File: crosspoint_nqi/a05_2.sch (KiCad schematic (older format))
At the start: 48 parts, among them U5022 74HC04, U5034 74HC27, U5035 74LVC07, U5036 74HC02, U5037 74HC4002, U5038 74HC02, U5039 74HC27, U5040 74HC27, U5041 74LVC07, U5042 74HC02, U5043 74HC27, U5044 74HC02, U5045 74HC27, U5046 74LVC07, U5047 74HC02, U5048 74HC27, U5049 74HC02, U5050 74HC02, U5051 74LVC07, U5052 74HC02, U5053 74HC02, U5054 74HC02, U5055 74HC4002, U5056 74HC27, U5057 74HC02, U5058 74LVC07, U5059 74HC04, U5060 74HC02, U5061 74LVC07, U5062 74HC02, U5063 74HC27, U5064 74HC27, U5065 74HC27, U5066 74HC02, U5067 74LVC07, U5068 74HC02, U5069 74HC27, U5070 74HC02

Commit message: Tied in module 6 and corrected a handful of naming/routing errors... most notably some missing gates from A06-1
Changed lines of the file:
@@
 	1    0    0    -1
 $EndComp
-Text Label 5650 10100 0    60   ~ 0
-5XP15
 Text Notes 5650 10200 0    60   ~ 0
 RG,WQ
@@
 	1    0    0    -1
 $EndComp
-Text Label 15800 4400 0    60   ~ 0
-6XP8
 Text Notes 15600 4550 0    60   ~ 0
 RU,WG,WSC,TOV
@@
 	16350 1350 17100 1350
 Connection ~ 16350 9300
+Wire Wire Line
+	5700 10100 5700 10000
+Wire Wire Line
+	5700 10000 5750 10000
+Connection ~ 5700 10100
+Text HLabel 5750 10000 2    60   Output ~ 0
+5XP15
+Wire Wire Line
+	15850 4400 15850 4300
+Wire Wire Line
+	15850 4300 15950 4300
+Connection ~ 15850 4400
+Text HLabel 15950 4300 2    60   Output ~ 0
+6XP8
 $EndSCHEMATC

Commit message: Tied in module 7, and corrected lots of errors.
Off the top of my head:
* T12DC/ not actually connected to restart logic in A02-2
* IC12/ and IC13 schematic errors
* Lots of gates moved from later modules up to modules 2-7
* YT0..7 logic dropped from 7, it belongs in 14
* Lots of missing signal breakouts
* ...probably some other things, I should keep a list as I go

All control pulses associated with GOJ1 now behave correctly during
GOJ1.
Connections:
- net CHINC/: now also U5049.8
- net T05/: now also U5044.12, U5044.9, U5047.12, U5047.3, U5047.9, U5049.12, U5049.3, U5049.6, U5049.9, U5050.3, U5050.6
- net RL10BB: now reaches U5034.9, U5036.10
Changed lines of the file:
@@
 Text HLabel 14300 7050 0    60   Input ~ 0
 MONWBK
-Text Label 16150 7050 2    60   ~ 0
-U2BBK
 $Comp
 L 74HC02 U5062
@@
 	4050 900  4450 900
 Wire Wire Line
-	6500 1000 5650 1000
+	5650 1000 6500 1000
 Wire Wire Line
 	8600 1150 8750 1150
@@
 	5650 6050 5650 6050
 Wire Wire Line
-	4400 7000 4400 11700
+	4400 5950 4400 11700
 Wire Wire Line
 	4400 6650 4450 6650
@@
 Connection ~ 4400 10200
 Wire Wire Line
-	4100 3150 4100 11500
+	4100 2100 4100 11500
 Wire Wire Line
 	4100 11500 4450 11500
@@
 	14600 7050 14300 7050
 Wire Wire Line
-	15800 7050 16150 7050
+	15800 7050 15900 7050
 Wire Wire Line
 	14550 6900 14550 7450
@@
 Text HLabel 15950 4300 2    60   Output ~ 0
 6XP8
+Wire Wire Line
+	6300 1000 6300 800
+Wire Wire Line
+	6300 800  6450 800
+Connection ~ 6300 1000
+Text HLabel 6450 800  2    60   Output ~ 0
+RL10BB
+Connection ~ 8750 6700
+Text HLabel 15900 7050 2    60   Output ~ 0
+U2BBK
 $EndSCHEMATC

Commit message: Tied in module 8, and corrected lots of initial conditions.
The registers and ALU appear to work now, with TC0 and STD2 shuffling things around correctly, and Z counting up as instructions execute.
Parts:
- U5039, U5040, U5045, U5047, U5050, U5055, U5057, U5059, U5064, U5070: Initial (none) -> 1
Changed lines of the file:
@@
 F 2 "" H 7250 3650 60  0000 C CNN
 F 3 "" H 7250 3650 60  0000 C CNN
+F 4 "1" H 7500 3650 60  0000 C CIN "Initial"
 	3    7250 3650
 	1    0    0    -1
@@
 F 2 "" H 7250 4100 60  0000 C CNN
 F 3 "" H 7250 4100 60  0000 C CNN
+F 4 "1" H 7500 4100 60  0000 C CIN "Initial"
 	1    7250 4100
 	1    0    0    -1
@@
 F 2 "" H 7250 8200 60  0000 C CNN
 F 3 "" H 7250 8200 60  0000 C CNN
+F 4 "1" H 7500 8200 60  0000 C CIN "Initial"
 	3    7250 8200
 	1    0    0    -1
@@
 F 2 "" H 7250 8750 60  0000 C CNN
 F 3 "" H 7250 8750 60  0000 C CNN
+F 4 "1" H 7500 8750 60  0000 C CIN "Initial"
 	2    7250 8750
 	1    0    0    -1
@@
 F 2 "" H 7250 9950 60  0000 C CNN
 F 3 "" H 7250 9950 60  0000 C CNN
+F 4 "1" H 7500 9950 60  0000 C CIN "Initial"
 	3    7250 9950
 	1    0    0    -1
@@
 F 2 "" H 17700 2750 60  0000 C CNN
 F 3 "" H 17700 2750 60  0000 C CNN
+F 4 "1" H 17950 2750 60  0000 C CIN "Initial"
 	4    17700 2750
 	1    0    0    -1
@@
 F 2 "" H 17550 3650 60  0000 C CNN
 F 3 "" H 17550 3650 60  0000 C CNN
+F 4 "1" H 17600 3650 60  0000 C CIN "Initial"
 	2    17550 3650
 	1    0    0    -1
@@
 F 2 "" H 17700 6050 60  0000 C CNN
 F 3 "" H 17700 6050 60  0000 C CNN
+F 4 "1" H 17950 6050 60  0000 C CIN "Initial"
 	2    17700 6050
 	1    0    0    -1
@@
 F 2 "" H 17700 8550 60  0000 C CNN
 F 3 "" H 17700 8550 60  0000 C CNN
+F 4 "1" H 17950 8550 60  0000 C CIN "Initial"
 	2    17700 8550
 	1    0    0    -1
@@
 F 2 "" H 17700 11350 60  0000 C CNN
 F 3 "" H 17700 11350 60  0000 C CNN
+F 4 "1" H 17950 11350 60  0000 C CIN "Initial"
 	3    17700 11350
 	1    0    0    -1

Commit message: Added and tied in module 12, parity & s register
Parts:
- U5034: Initial (none) -> 1
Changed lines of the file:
@@
 F 2 "" H 7100 1150 60  0000 C CNN
 F 3 "" H 7100 1150 60  0000 C CNN
+F 4 "1" H 7350 1150 60  0000 C CIN "Initial"
 	3    7100 1150
 	1    0    0    -1

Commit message: Bux fixes for things found during FPGA integration.
* A05 was driving TSGN/ directly instead of with an OD buffer+pullup
* Some bad logic with crosspoints in module 5
* A bad part number in module 12
* Removal of unused signals from the backplane connectors
* Addition of some monitor signals from the timer to the backplane
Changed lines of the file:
@@
 $EndComp
 $Comp
-L VCC #PWR04
+L VCC #PWR05
 U 1 1 5688CD87
 P 3500 750
-F 0 "#PWR04" H 3500 600 50  0001 C CNN
+F 0 "#PWR05" H 3500 600 50  0001 C CNN
 F 1 "VCC" H 3500 900 50  0000 C CNN
 F 2 "" H 3500 750 60  0000 C CNN
@@
 $EndComp
 $Comp
-L VCC #PWR05
+L VCC #PWR06
 U 1 1 56896A8F
 P 3500 3250
-F 0 "#PWR05" H 3500 3100 50  0001 C CNN
+F 0 "#PWR06" H 3500 3100 50  0001 C CNN
 F 1 "VCC" H 3500 3400 50  0000 C CNN
 F 2 "" H 3500 3250 60  0000 C CNN
@@
 $EndComp
 $Comp
-L VCC #PWR06
+L VCC #PWR07
 U 1 1 568A00F6
 P 8750 4700
-F 0 "#PWR06" H 8750 4550 50  0001 C CNN
+F 0 "#PWR07" H 8750 4550 50  0001 C CNN
 F 1 "VCC" H 8750 4850 50  0000 C CNN
 F 2 "" H 8750 4700 60  0000 C CNN
@@
 $EndComp
 $Comp
-L VCC #PWR07
+L VCC #PWR08
 U 1 1 568A6D55
 P 8750 5400
-F 0 "#PWR07" H 8750 5250 50  0001 C CNN
+F 0 "#PWR08" H 8750 5250 50  0001 C CNN
 F 1 "VCC" H 8750 5550 50  0000 C CNN
 F 2 "" H 8750 5400 60  0000 C CNN
@@
 $EndComp
 $Comp
-L VCC #PWR08
+L VCC #PWR09
 U 1 1 568CC1CC
 P 8750 7850
-F 0 "#PWR08" H 8750 7700 50  0001 C CNN
+F 0 "#PWR09" H 8750 7700 50  0001 C CNN
 F 1 "VCC" H 8750 8000 50  0000 C CNN
 F 2 "" H 8750 7850 60  0000 C CNN
@@
 $EndComp
 $Comp
-L VCC #PWR09
+L VCC #PWR010
 U 1 1 568E968F
 P 8750 9600
-F 0 "#PWR09" H 8750 9450 50  0001 C CNN
+F 0 "#PWR010" H 8750 9450 50  0001 C CNN
 F 1 "VCC" H 8750 9750 50  0000 C CNN
 F 2 "" H 8750 9600 60  0000 C CNN
@@
 $EndComp
 $Comp
-L VCC #PWR010
+L VCC #PWR011
 U 1 1 568F254F
 P 3950 12200
-F 0 "#PWR010" H 3950 12050 50  0001 C CNN
+F 0 "#PWR011" H 3950 12050 50  0001 C CNN
 F 1 "VCC" H 3950 12350 50  0000 C CNN
 F 2 "" H 3950 12200 60  0000 C CNN
@@
 $EndComp
 $Comp
-L VCC #PWR011
+L VCC #PWR012
 U 1 1 5693179F
 P 13850 2200
-F 0 "#PWR011" H 13850 2050 50  0001 C CNN
+F 0 "#PWR012" H 13850 2050 50  0001 C CNN
 F 1 "VCC" H 13850 2350 50  0000 C CNN
 F 2 "" H 13850 2200 60  0000 C CNN
@@
 $EndComp
 $Comp
-L VCC #PWR012
+L VCC #PWR013
 U 1 1 5695184C
 P 18900 8950
-F 0 "#PWR012" H 18900 8800 50  0001 C CNN
+F 0 "#PWR013" H 18900 8800 50  0001 C CNN
 F 1 "VCC" H 18900 9100 50  0000 C CNN
 F 2 "" H 18900 8950 60  0000 C CNN
@@
 $EndComp
 $Comp
-L VCC #PWR013
+L VCC #PWR014
 U 1 1 569C69D1
 P 13850 3400
-F 0 "#PWR013" H 13850 3250 50  0001 C CNN
+F 0 "#PWR014" H 13850 3250 50  0001 C CNN
 F 1 "VCC" H 13850 3550 50  0000 C CNN
 F 2 "" H 13850 3400 60  0000 C CNN
@@
 	19200 11350 19300 11350
 Wire Wire Line
-	16300 7750 17100 7750
+	15950 7750 17100 7750
 Wire Wire Line
 	16950 7750 16950 11250
@@
 	16950 11250 17100 11250
 Connection ~ 16950 7750
-Text HLabel 16300 7750 0    60   Input ~ 0
-5XP9
 $Comp
 L 74HC02 U5070
@@
 Text HLabel 15900 7050 2    60   Output ~ 0
 U2BBK
+Text Label 15950 7750 0    60   ~ 0
+5XP9
 $EndSCHEMATC

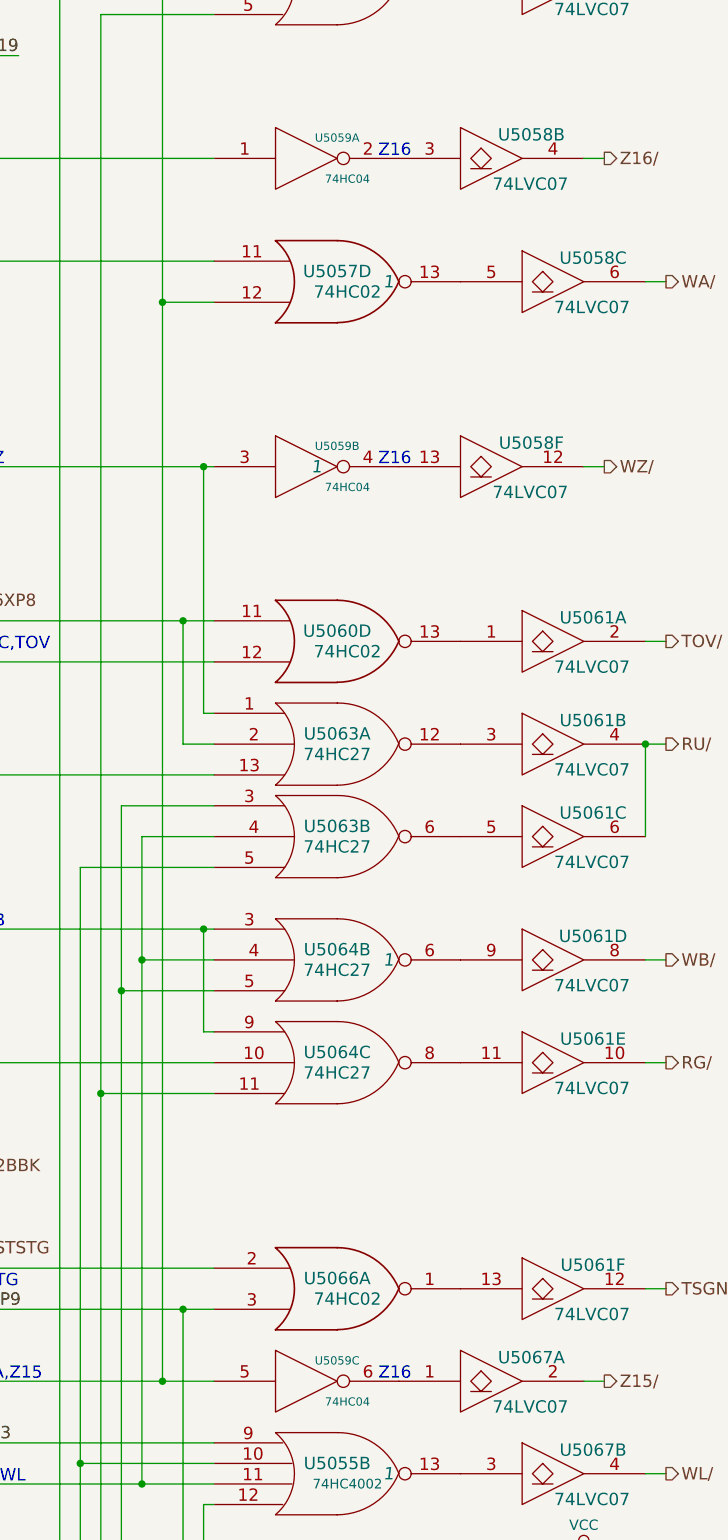
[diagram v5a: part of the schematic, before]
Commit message: Finished off and integrated module 14. Also fixed a couple of bugs this turned up (both initial conditions, and bad wiring in the CGMC pulse generator and S register)
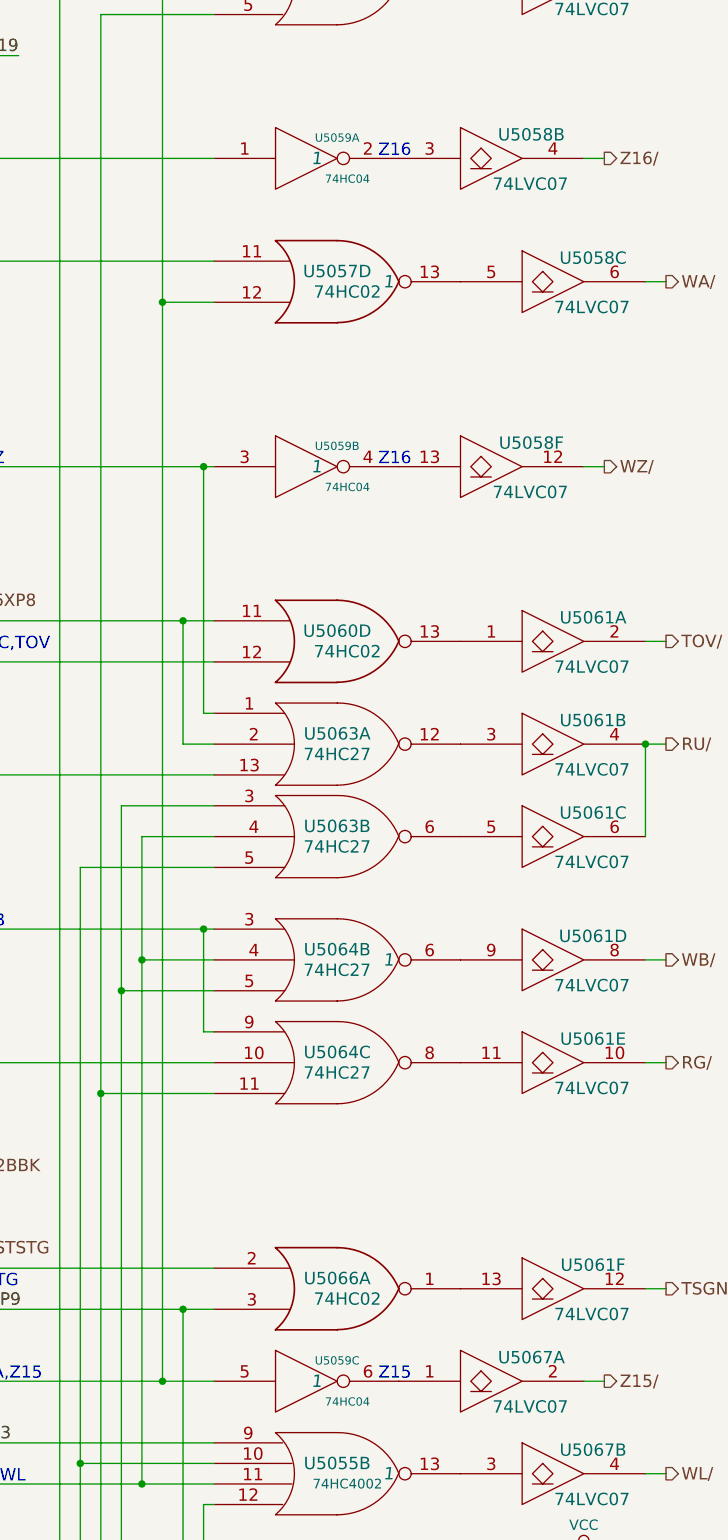
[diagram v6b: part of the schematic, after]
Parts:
- U5059: Initial (none) -> 1
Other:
- note added: "Z15"
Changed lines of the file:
@@
 F 2 "" H 17550 2150 60  0000 C CNN
 F 3 "" H 17550 2150 60  0000 C CNN
+F 4 "1" H 17600 2150 60  0000 C CIN "Initial"
 	1    17550 2150
 	1    0    0    -1
@@
 F 2 "" H 17550 8100 60  0000 C CNN
 F 3 "" H 17550 8100 60  0000 C CNN
+F 4 "1" H 17600 8100 60  0000 C CIN "Initial"
 	3    17550 8100
 	1    0    0    -1
@@
 $EndComp
 Text Notes 17900 8100 0    60   ~ 0
-Z16
+Z15
 Wire Wire Line
 	15800 8100 17100 8100

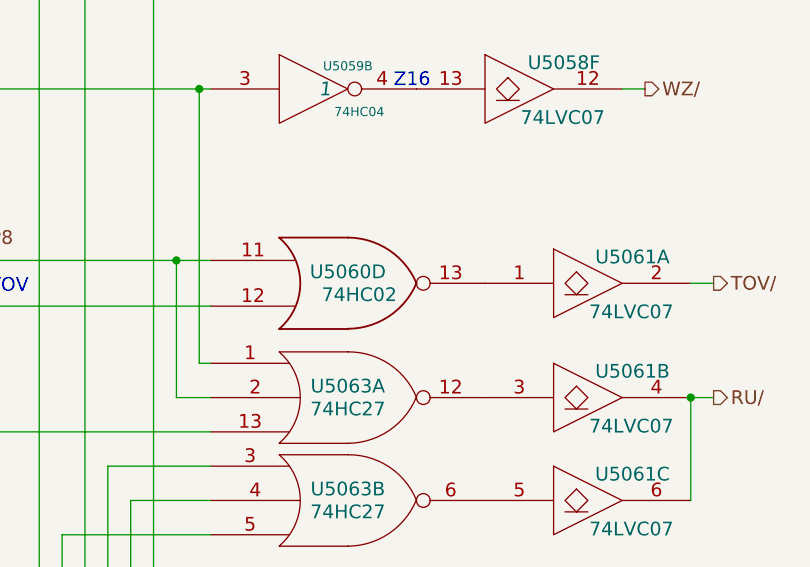
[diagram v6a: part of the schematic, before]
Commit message: Added erasable memory, and fixed lots of random wiring errors.
I decided to go with a 16-bit-wide MRAM chip -- I had  no idea
until I started researching RAM options how technologically
similar MRAM is to core memory. The datasheet diagrams look like
they're straight out of the AGC documentation!

There's a slight inaccuracy in this implementation worth mentioning.
Like fixed memory, I've wired the sense amplifier outputs directly up
to the tristate data output pins of the MRAM chip. But because the
data lines are bidirectional, data being written into RAM will show up
on the sense lines, and go straight into the ungated G register. Since
G is what's being written out, this doesn't matter 99% of the time, but
if there's an overflow condition in G (I don't even know if this is
possible), the bit 16 will be copied over bit 16, and the overflow
condition will be lost. I'll keep an eye out to see if anything relies
on G not changing after the write cycle is complete.

With erasable memory introduced, the computer now theoretically supports
all programs that don't use I/O or interrupts. I've started running
the VirtualAGC validation program, and have been fixing random errors
uncovered by failing self-tests.
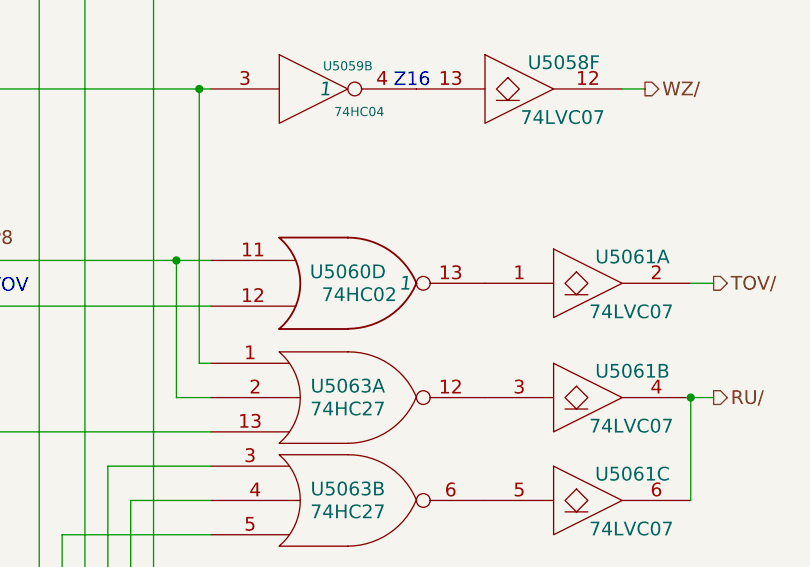
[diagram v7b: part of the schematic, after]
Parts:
- U5060: Initial (none) -> 1
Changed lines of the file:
@@
 F 2 "" H 17700 4500 60  0000 C CNN
 F 3 "" H 17700 4500 60  0000 C CNN
+F 4 "1" H 17950 4500 60  0000 C CIN "Initial"
 	4    17700 4500
 	1    0    0    -1
